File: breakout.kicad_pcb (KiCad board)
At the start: 2 copper layers, 50 x 50 mm, 34 parts, among them J1 JACK_TRS_4PINS, P1 CONN_01X08, P2 SPEAKER, P3 ISO7816_SIMPLE, P4 CONN_01X09, P5 SMA_CONN, P6 MIC, P7 USB_A, Q1 Q_PMOS_GSD, Q2 Q_NMOS_GSD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

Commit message: Bump version.
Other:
- board text added: "v0.5 GSM Board"
- board text removed: "v0.4 GSM Board"
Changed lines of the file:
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@@
     (links 96)
     (no_connects 0)
-    (area 149.924999 49.924999 200.075001 100.075001)
+    (area 147.900458 46.4 204.415 100.425001)
     (thickness 1.6)
     (drawings 51)
@@
     (effects (font (size 1 1) (thickness 0.25)) (justify right mirror))
   )
-  (gr_text "v0.4 GSM\nBoard\n" (at 192.75 92.51) (layer F.SilkS)
+  (gr_text "v0.5 GSM\nBoard\n" (at 192.75 92.51) (layer F.SilkS)
     (effects (font (size 1 1) (thickness 0.25)))
   )

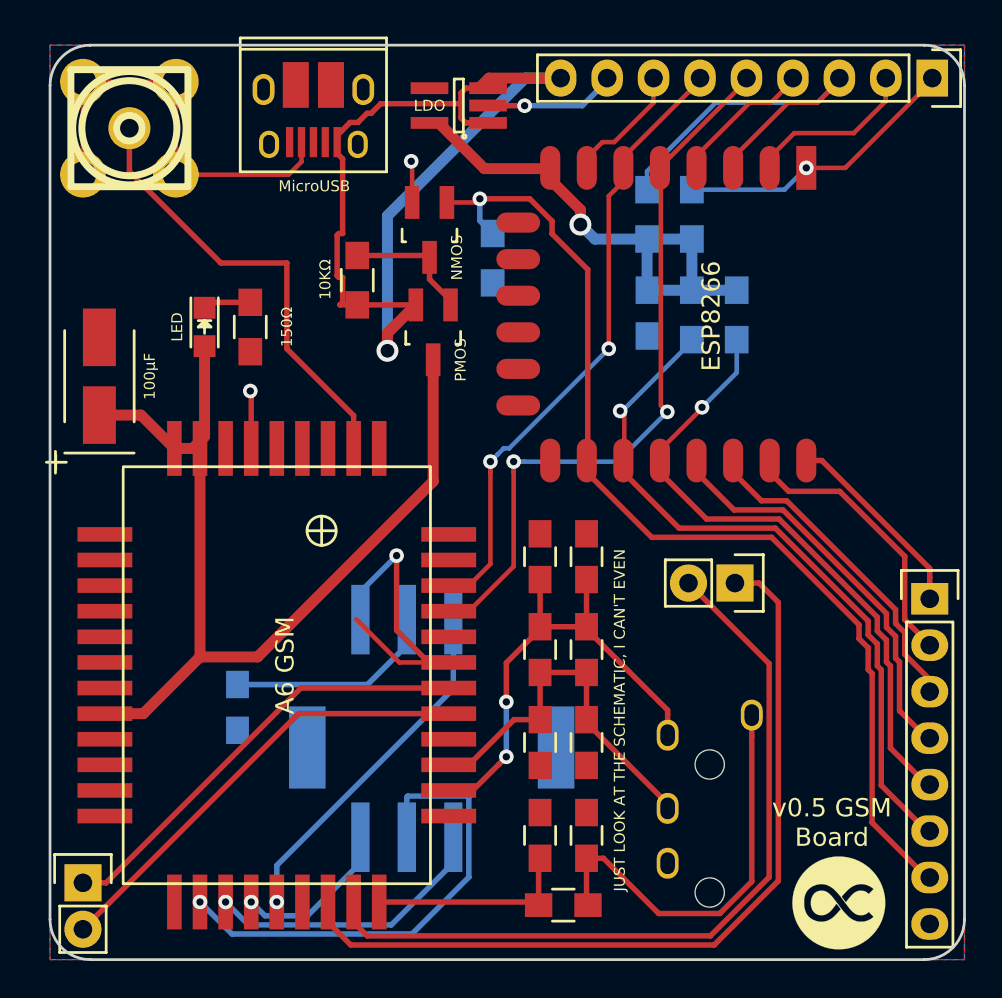
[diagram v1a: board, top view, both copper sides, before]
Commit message: Add inductors for audio.
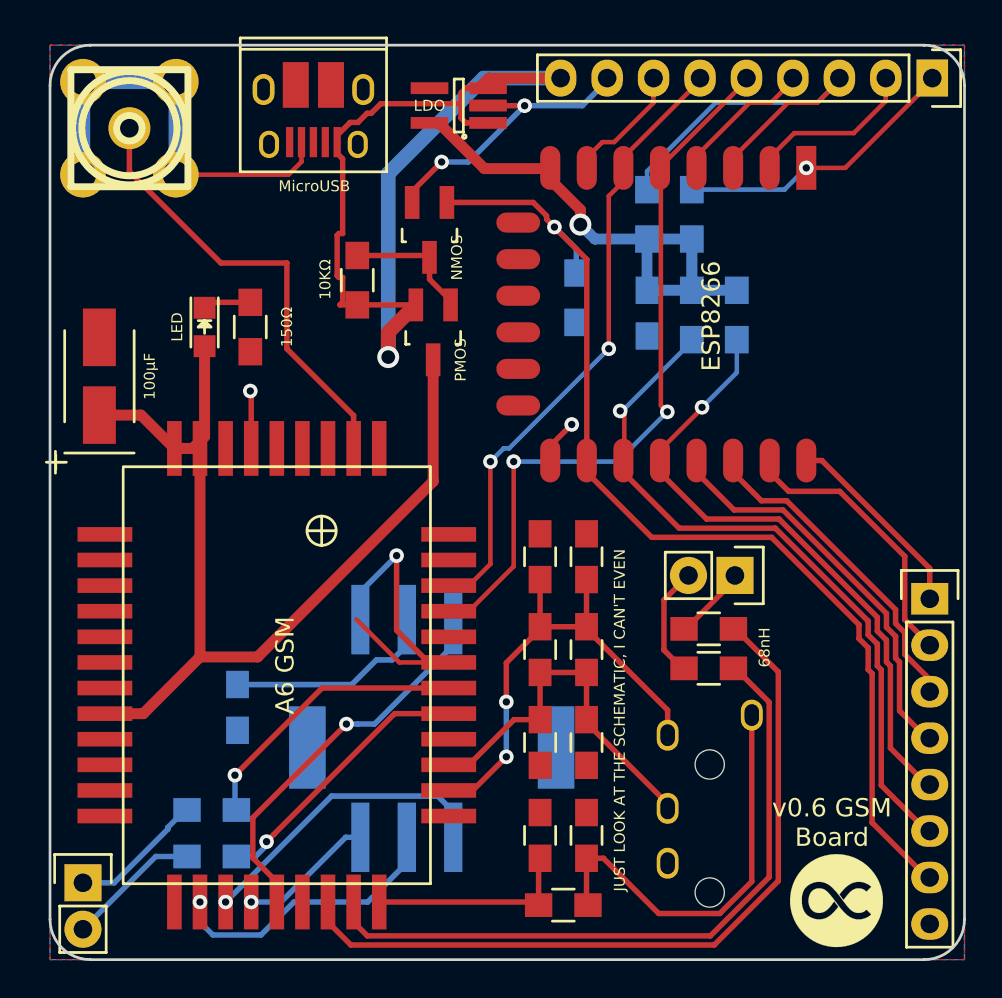
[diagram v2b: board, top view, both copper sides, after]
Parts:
- removed LOGO: LOGO, Stochastic:Logo_5mm
- added G***: LOGO, Stochastic:Logo_5mm, F.Cu at (193.0, 96.8)
- added L1: 68nH, Resistors_SMD:R_0805_HandSoldering, F.Cu at (186.0, 81.9)
- added L2: 68nH, Resistors_SMD:R_0805_HandSoldering, F.Cu at (186.0, 84.1)
- added L3: 68nH, Resistors_SMD:R_0805_HandSoldering, B.Cu at (158.8, 91.8)
- added L4: 68nH, Resistors_SMD:R_0805_HandSoldering, B.Cu at (158.8, 94.4)
- moved R4 5.06 mm to (178.8, 63.8)
- moved P6 0.42 mm to (187.4, 79.0)
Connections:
- P2 pad 1: Net-(GSM1-Pad27) -> Net-(L3-Pad1)
- P2 pad 2: Net-(GSM1-Pad26) -> Net-(L4-Pad1)
- P6 pad 1: Net-(GSM1-Pad19) -> Net-(L1-Pad2)
- P6 pad 2: Net-(GSM1-Pad20) -> Net-(L2-Pad2)
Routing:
- net Net-(GSM1-Pad14): track 26.7 -> 15.7 mm
- net Net-(GSM1-Pad26): track 24.9 -> 15.0 mm, vias 0 -> 1
- net GND: track 54.6 -> 63.5 mm, vias 4 -> 5
- net Net-(GSM1-Pad27): track 24.4 -> 15.6 mm, vias 0 -> 1
- net Net-(L3-Pad1): track 0.00 -> 7.40 mm
- net Net-(L4-Pad1): track 0.00 -> 7.34 mm
- net Net-(L2-Pad2): track 0.00 -> 6.15 mm
- net Net-(GSM1-Pad20): track 43.4 -> 37.7 mm
- net Net-(L1-Pad2): track 0.00 -> 4.13 mm
- net Net-(GSM1-Pad19): track 45.7 -> 42.5 mm
- net Net-(GSM1-Pad17): track 19.4 -> 21.4 mm
- net VCC: track 51.9 -> 53.9 mm
- net Net-(GSM1-Pad16): track 8.88 -> 7.44 mm
- net Net-(GSM1-Pad15): track 15.8 -> 16.6 mm
- net /PWRCTL: track 57.0 -> 57.6 mm
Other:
- board text added: "68nH"
- board text added: "v0.6 GSM Board"
- board text removed: "v0.5 GSM Board"

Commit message: Fix USB pin issue.
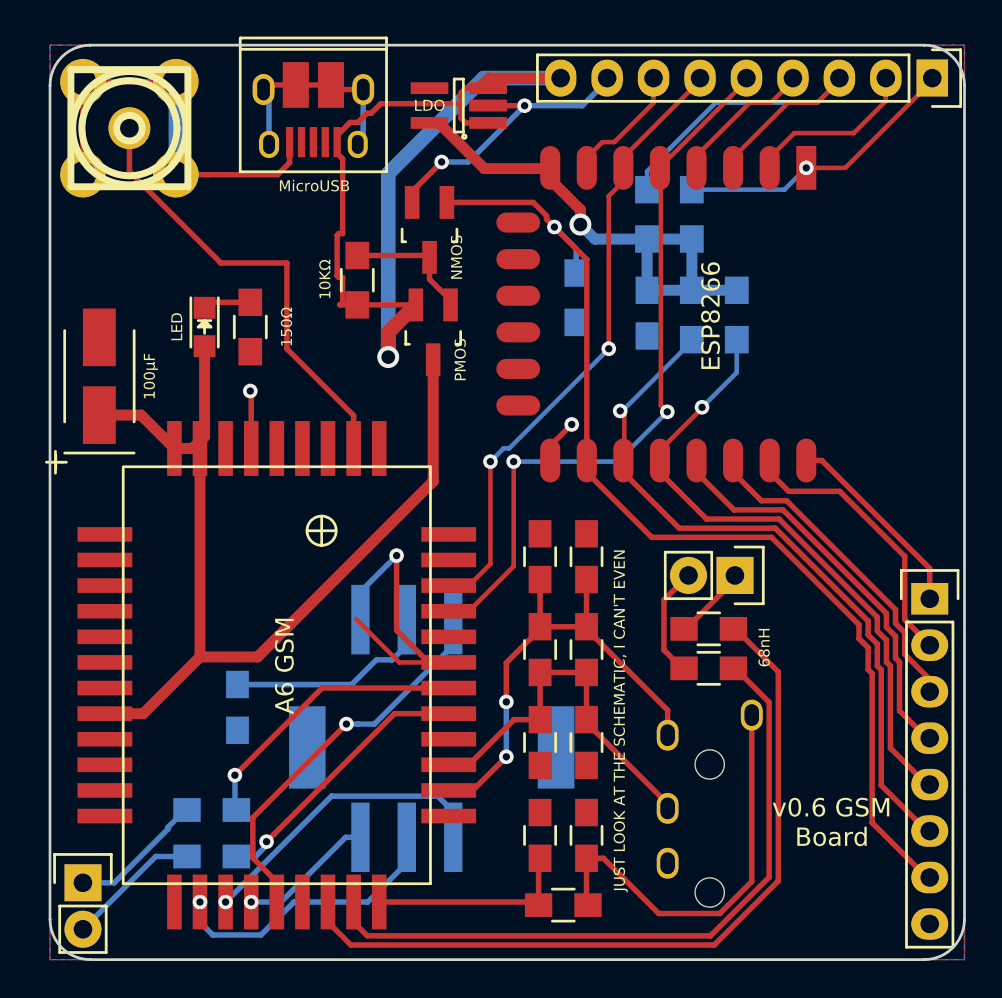
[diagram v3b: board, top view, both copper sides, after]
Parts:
- removed G***: LOGO, Stochastic:Logo_5mm
- P7: value USB_A -> USB_OTG
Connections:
- P7 pad 4: GND -> (no net)
- P7 pad 5: (no net) -> GND
- P7 pad 6: (no net) -> Net-(P7-Pad6)
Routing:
- net Net-(P7-Pad6): track 0.00 -> 11.9 mm
- net GND: track 63.5 -> 62.9 mm

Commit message: Add Stochastic logo.
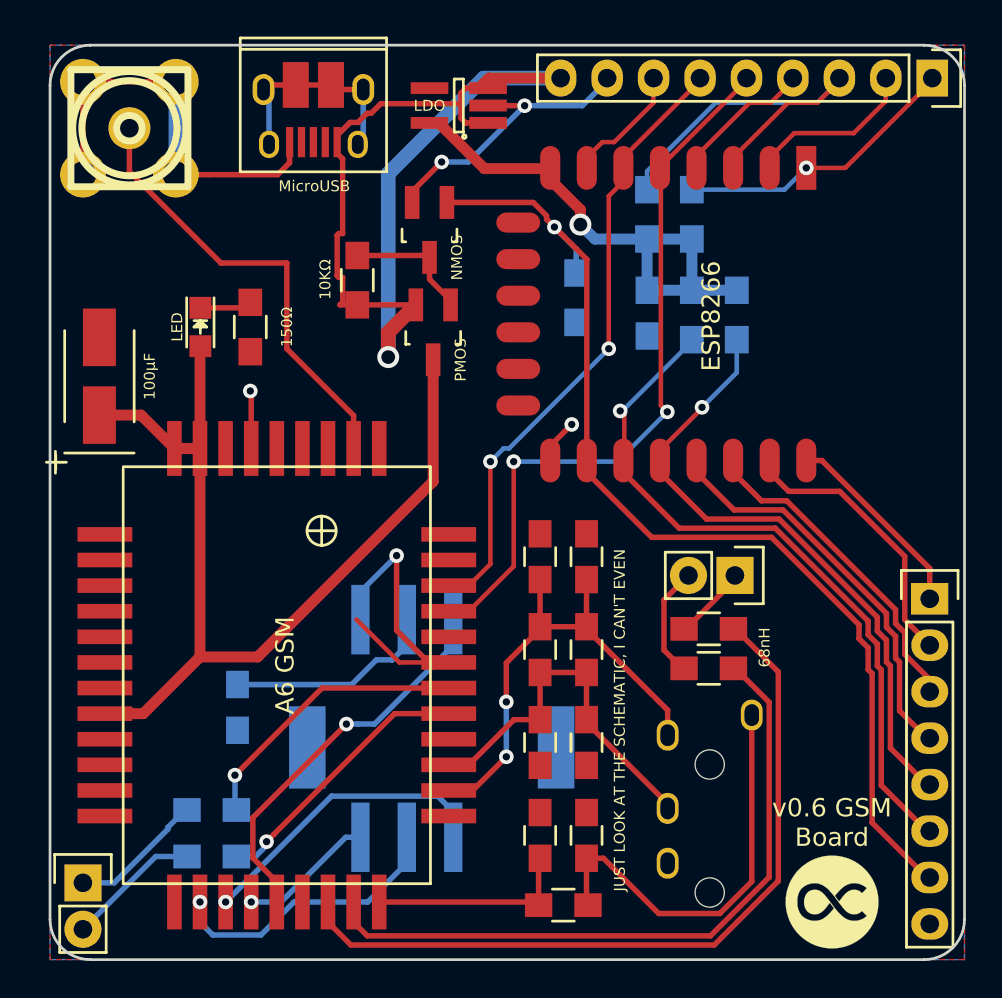
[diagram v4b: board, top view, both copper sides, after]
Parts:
- added G***: LOGO, Stochastic:Logo_5mm, F.Cu at (192.8, 96.8)
- moved D1 0.23 mm to (158.2, 65.4)

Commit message: Various fixes.
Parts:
- moved L3 7.65 mm to (151.4, 89.9), turned to 90 degrees
- moved L4 6.62 mm to (154.0, 89.9), turned to 90 degrees
- moved C4 1.25 mm to (159.0, 86.1)
- moved P3 0.38 mm to (179.2, 97.4)
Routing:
- net Net-(GSM1-Pad26): track 15.0 -> 36.8 mm
- net Net-(GSM1-Pad27): track 15.6 -> 31.8 mm
- net Net-(GSM1-Pad17): track 21.4 -> 29.3 mm
- net Net-(C4-Pad2): track 11.6 -> 16.6 mm
- net VCC: track 53.9 -> 49.3 mm
- net /3V3: track 27.8 -> 30.8 mm
- net Net-(L3-Pad1): track 7.40 -> 4.73 mm
- net Net-(GSM1-Pad14): track 15.7 -> 16.8 mm
- net GND: track 62.9 -> 62.1 mm, vias 5 -> 3
- net Net-(L4-Pad1): track 7.34 -> 8.02 mm
- net Net-(GSM1-Pad15): track 16.6 -> 17.2 mm
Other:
- board text added: "v0.7 GSM Board"
- board text removed: "v0.6 GSM Board"

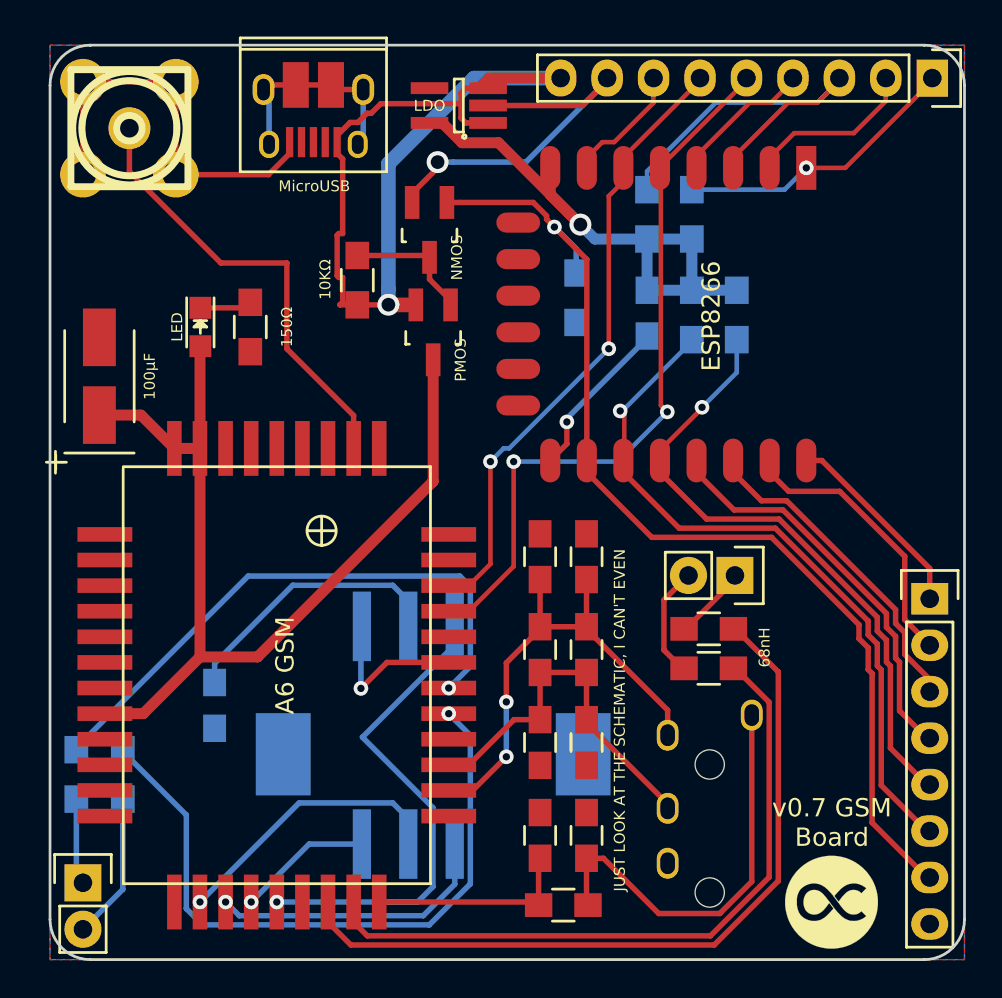
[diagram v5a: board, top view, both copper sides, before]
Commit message: Change A6 TX/RX pins.
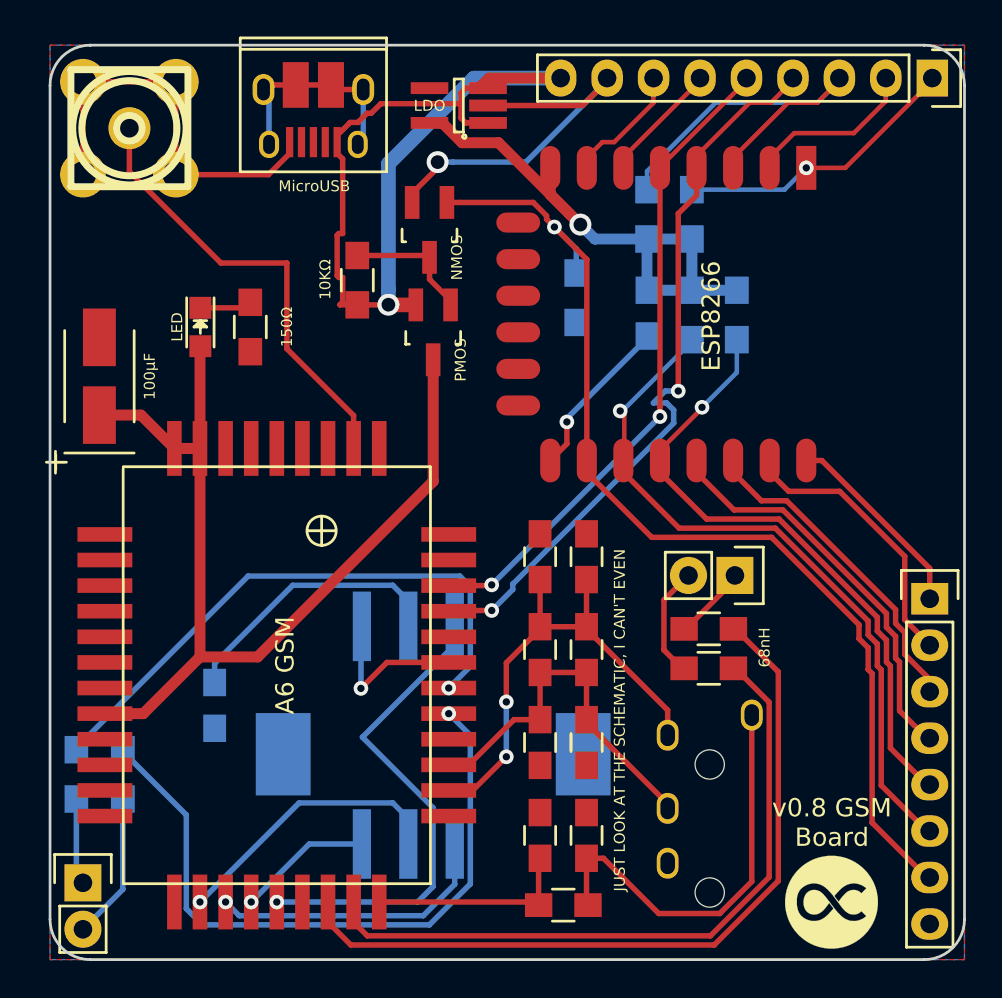
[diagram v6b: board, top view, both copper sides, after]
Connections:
- net VCC renamed /Vcc
- P4 pad 4: /GPIO16 -> /ESP_RX
- P4 pad 5: /ESP_RX -> /ESP_TX
- P4 pad 6: /ESP_TX -> /GPIO12
- U2 pad 4: /GPIO16 -> /ESP_RX
- U2 pad 5: /ESP_RX -> /ESP_TX
- U2 pad 6: /ESP_TX -> /GPIO12
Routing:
- net /GPIO16: track 7.79 -> 0.00 mm
- net /GPIO12: track 0.00 -> 7.31 mm
- net /ESP_TX: track 34.3 -> 37.0 mm
- net /ESP_RX: track 40.2 -> 40.8 mm
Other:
- board text added: "v0.8 GSM Board"
- board text removed: "v0.7 GSM Board"
